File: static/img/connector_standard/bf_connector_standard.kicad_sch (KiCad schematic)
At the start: 11 parts, among them J1 ESC Connector, J10 UART + I2C Connector, J11 3-pin Camera Connector, J2 I2C Connector, J3 Analog VTX Connector, J4 Extended ESC Connector, J5 5-pin Camera Connector, J6 Digital VTX Connector, J7 UART Connector, J8 4-pin Camera Connector, J9 SWD Connector

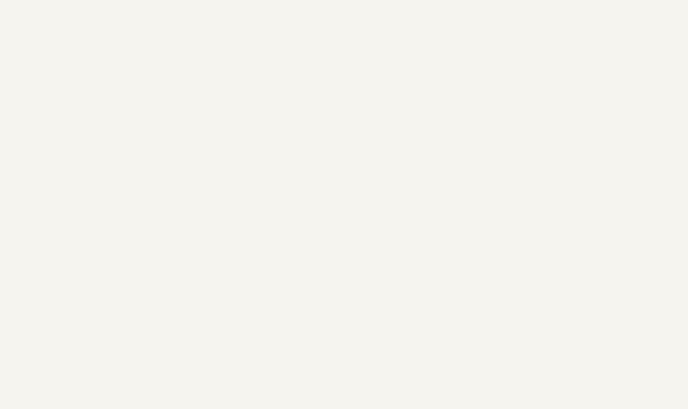
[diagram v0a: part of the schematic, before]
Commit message: docs(connector-standard): add FDCAN connector (v2.2)
Adds the 4-pin FDCAN connector, adopting the CAN connector of the PX4 and
ArduPilot connector standard unchanged: JST GH 1.25 mm, pin 1 +5V, 2 CAN_H,
3 CAN_L, 4 GND.

The pin order deliberately differs from the rest of this standard (ground on
pin 4, not pin 2) because the pinout is taken from the Pixhawk standard rather
than defined here. Correcting it would break compatibility with every existing
CAN peripheral, so the caution note calls this out explicitly.

Reframes the JST SH/GH sections so that adopting an established external
standard reads as deliberate practice rather than an awkward exception: a
competing Betaflight CAN pinout would fragment the peripheral and harness
supply this document exists to unify. JST GH is therefore not optional for
FDCAN, even on a board that is otherwise entirely JST SH.

Adds the connector to the reference schematic as J12 and regenerates the
complete schematic SVG and PDF from it.
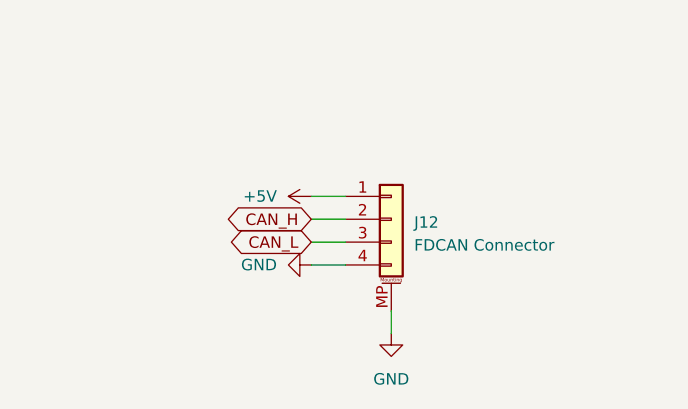
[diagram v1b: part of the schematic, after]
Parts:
- added J12: FDCAN Connector, Connector_JST:JST_GH_SM04B-GHS-TB_1x04-1MP_P1.25mm_Horizontal, symbol Connector_Generic_MountingPin:Conn_01x04_MountingPin
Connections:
- net +5V: now also J12.1 (Pin_1)
- net GND: now also J12.4 (Pin_4), J12.MP (MountPin)
- new net CAN_H: J12.2 (Pin_2)
- new net CAN_L: J12.3 (Pin_3)
